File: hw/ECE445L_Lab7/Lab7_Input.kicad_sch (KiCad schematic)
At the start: 23 parts, among them Q16 NTR4501NT1G, Q17 NTR4501NT1G

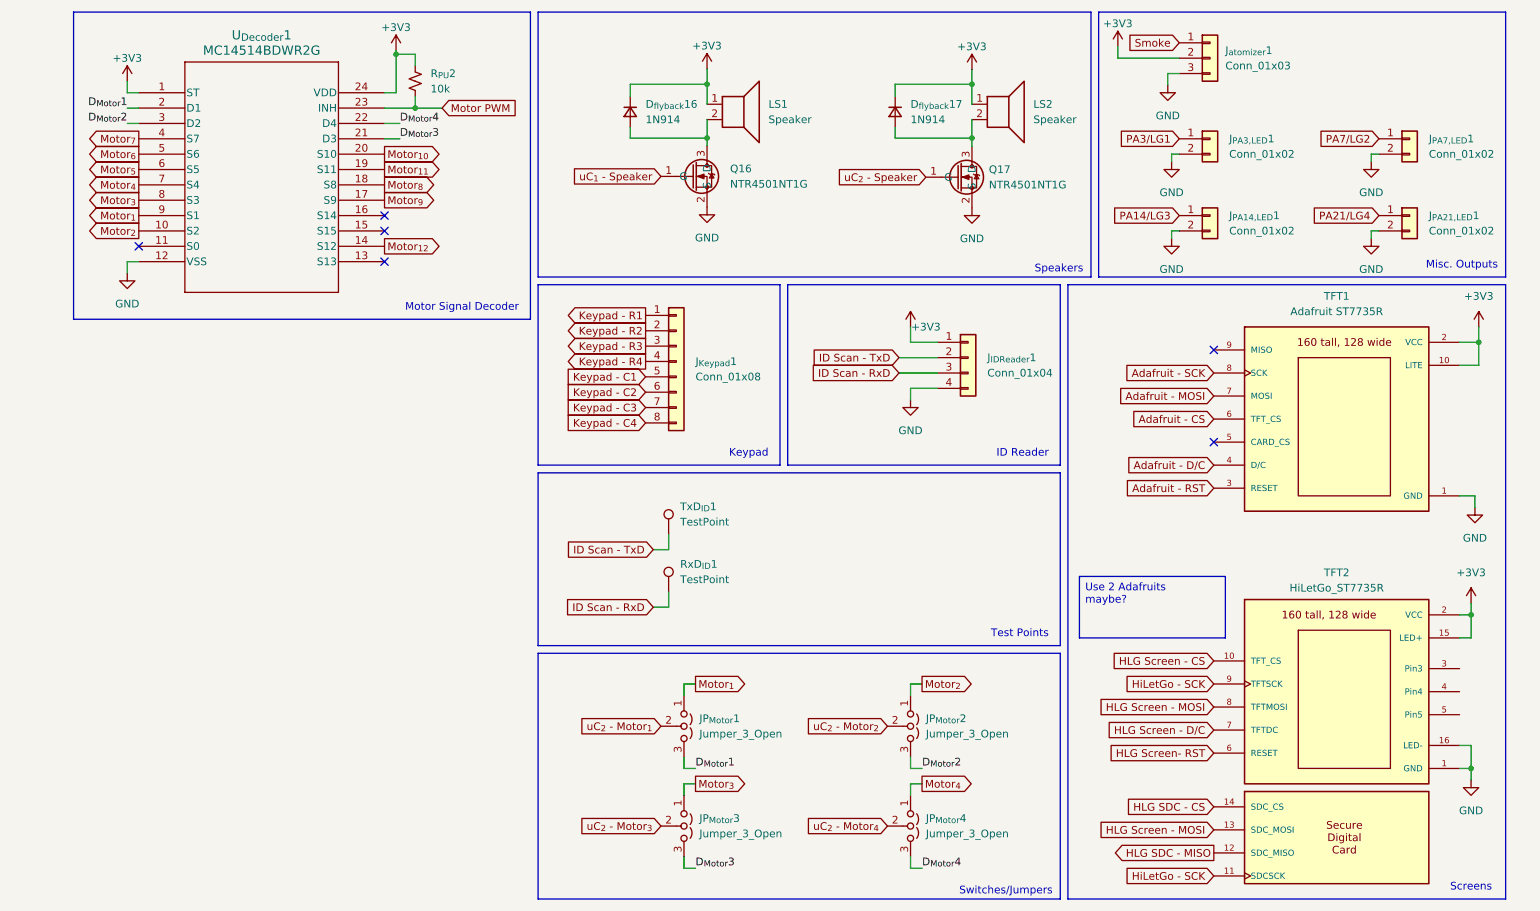
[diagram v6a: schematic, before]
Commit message: started pcb layout
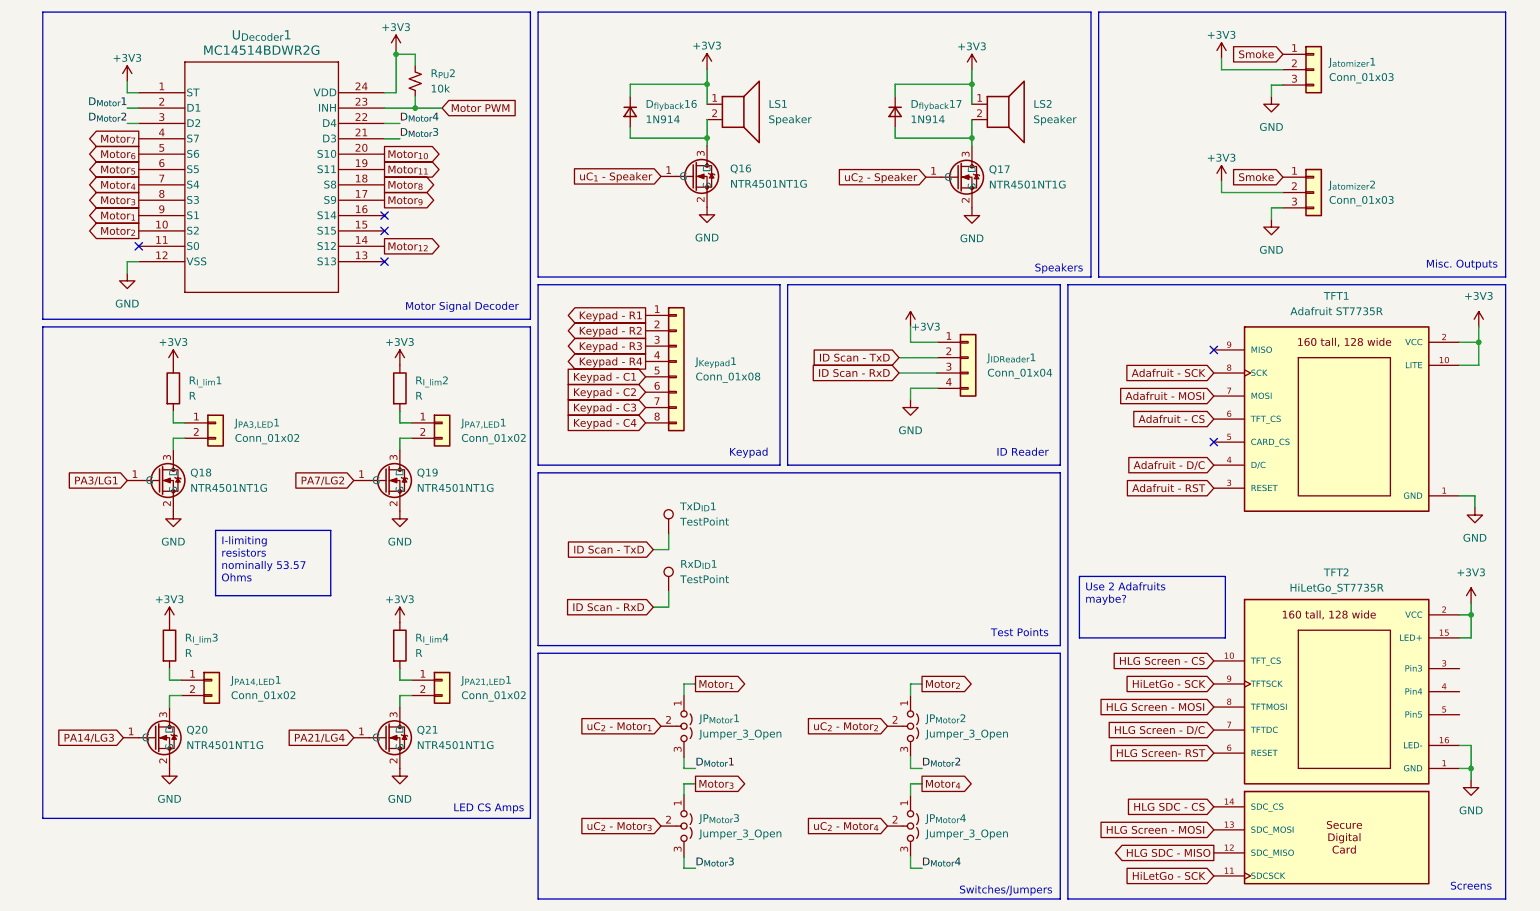
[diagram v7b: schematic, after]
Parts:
- added J_{atomizer}2: Conn_01x03, Connector_PinSocket_2.54mm:PinSocket_1x03_P2.54mm_Vertical, symbol Connector_Generic:Conn_01x03
- added Q18, Q19, Q20, Q21: NTR4501NT1G, ECE445L:SOT96P237X111-3N, symbol ECE445L:NTR4501NT1G
- added R_{I_lim}1, R_{I_lim}2, R_{I_lim}3, R_{I_lim}4: R, Resistor_SMD:R_0603_1608Metric_Pad0.98x0.95mm_HandSolder, symbol Device:R
- D_{flyback}16, D_{flyback}17: footprint Diode_THT:D_5W_P12.70mm_Horizontal -> Diode_SMD:D_SOD-882D
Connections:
- net +3V3: now also J_{atomizer}2.2 (Pin_2), R_{I_lim}1.1, R_{I_lim}2.1, R_{I_lim}3.1, R_{I_lim}4.1
- net GND: now also J_{atomizer}2.3 (Pin_3), Q18.2 (S), Q19.2 (S), Q20.2 (S), Q21.2 (S); no longer J_{PA14,LED}1.2 (Pin_2), J_{PA21,LED}1.2 (Pin_2), J_{PA3,LED}1.2 (Pin_2), J_{PA7,LED}1.2 (Pin_2)
- net PA14/LG3: now also Q20.1 (G); no longer J_{PA14,LED}1.1 (Pin_1)
- net PA21/LG4: now also Q21.1 (G); no longer J_{PA21,LED}1.1 (Pin_1)
- net PA3/LG1: now also Q18.1 (G); no longer J_{PA3,LED}1.1 (Pin_1)
- net PA7/LG2: now also Q19.1 (G); no longer J_{PA7,LED}1.1 (Pin_1)
- net Smoke: now also J_{atomizer}2.1 (Pin_1)
- new net: J_{PA7,LED}1.2 (Pin_2), Q19.3 (D)
- new net: J_{PA14,LED}1.1 (Pin_1), R_{I_lim}3.2
- new net: J_{PA3,LED}1.1 (Pin_1), R_{I_lim}1.2
- new net: J_{PA21,LED}1.1 (Pin_1), R_{I_lim}4.2
- new net: J_{PA21,LED}1.2 (Pin_2), Q21.3 (D)
- new net: J_{PA14,LED}1.2 (Pin_2), Q20.3 (D)
- new net: J_{PA3,LED}1.2 (Pin_2), Q18.3 (D)
- new net: J_{PA7,LED}1.1 (Pin_1), R_{I_lim}2.2
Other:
- note added: "LED CS Amps"
- moved on the sheet: J_{PA14,LED}1, J_{PA21,LED}1, J_{PA3,LED}1, J_{PA7,LED}1, J_{atomizer}1

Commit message: handoff to jonathan until midnight
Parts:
- D_{flyback}16, D_{flyback}17: value 1N914 -> PE1403M1Q
- Q16, Q17, Q18, Q19, Q20, Q21: Distributor Checkout -> Valvano
- R_{I_lim}1, R_{I_lim}2, R_{I_lim}3, R_{I_lim}4: Distributor (none) -> Valvano
- R_{PU}2: Distributor Mouser -> Valvano
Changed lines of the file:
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@@
 			)
 		)
-		(property "Distributor" "Checkout"
+		(property "Distributor" "Valvano"
 			(at 91.44 92.71 0)
 			(hide yes)
@@
 			)
 		)
+		(property "Distributor" "Valvano"
+			(at 60.96 120.015 0)
+			(hide yes)
+			(show_name no)
+			(do_not_autoplace no)
+			(effects
+				(font
+					(size 1.27 1.27)
+				)
+			)
+		)
 		(pin "2"
 		)
@@
 			)
 		)
+		(property "Distributor" "Valvano"
+			(at 61.595 77.47 0)
+			(hide yes)
+			(show_name no)
+			(do_not_autoplace no)
+			(effects
+				(font
+					(size 1.27 1.27)
+				)
+			)
+		)
 		(pin "2"
 		)
@@
 			)
 		)
+		(property "Distributor" "Valvano"
+			(at 99.06 120.015 0)
+			(hide yes)
+			(show_name no)
+			(do_not_autoplace no)
+			(effects
+				(font
+					(size 1.27 1.27)
+				)
+			)
+		)
 		(pin "2"
 		)
@@
 			)
 		)
-		(property "Distributor" "Checkout"
+		(property "Distributor" "Valvano"
 			(at 91.44 135.255 0)
 			(hide yes)
@@
 			)
 		)
-		(property "Value" "1N914"
+		(property "Value" "PE1403M1Q"
 			(at 183.515 33.0199 90)
 			(show_name no)
@@
 			)
 		)
-		(property "Distributor" "Mouser"
+		(property "Distributor" "Valvano"
 			(at 101.6 26.67 0)
 			(hide yes)
@@
 			)
 		)
-		(property "Distributor" "Checkout"
+		(property "Distributor" "Valvano"
 			(at 53.34 135.255 0)
 			(hide yes)
@@
 			)
 		)
-		(property "Distributor" "Checkout"
+		(property "Distributor" "Valvano"
 			(at 53.975 92.71 0)
 			(hide yes)
@@
 			)
 		)
-		(property "Distributor" "Checkout"
+		(property "Distributor" "Valvano"
 			(at 142.24 42.418 0)
 			(hide yes)
@@
 			)
 		)
-		(property "Value" "1N914"
+		(property "Value" "PE1403M1Q"
 			(at 139.7 33.0199 90)
 			(show_name no)
@@
 			)
 		)
+		(property "Distributor" "Valvano"
+			(at 99.06 77.47 0)
+			(hide yes)
+			(show_name no)
+			(do_not_autoplace no)
+			(effects
+				(font
+					(size 1.27 1.27)
+				)
+			)
+		)
 		(pin "2"
 		)
@@
 			)
 		)
-		(property "Distributor" "Checkout"
+		(property "Distributor" "Valvano"
 			(at 186.055 42.545 0)
 			(hide yes)
